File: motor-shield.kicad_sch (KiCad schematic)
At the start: 73 parts, among them J101 MC 1,5/ 2-G-3,5, J102 -, J103 MC 1,5/ 2-G-3,5, J104 -, J105 STEMMA QT, J106 Conn_02x04_smd, J107 Conn_01x04_f, Q101 AO3400A, Q102 AO3400A, SW101 Switch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

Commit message: Update to RevA1
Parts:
- removed FID101, FID102, FID103: Toolinghole_jlc, _my:toolinghole_jlc, symbol _my:Toolinghole_jlc
- removed FID104, FID105, FID106: Fiducial, Fiducial:Fiducial_1mm_Mask2mm, symbol Mechanical:Fiducial
- A101: footprint Module:Arduino_UNO_R3 -> _my:Arduino_UNO_R3_edit
- J107: footprint Connector_PinSocket_2.54mm:PinSocket_1x04_P2.54mm_Vertical -> _my:PinHeader_1x04_P2.54mm_Vertical_solderpad
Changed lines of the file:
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@@
     )
   )
-  (symbol (lib_id "_my:Toolinghole_jlc") (at 274.32 248.92 0) (unit 1)
-    (in_bom yes) (on_board yes) (dnp no) (fields_autoplaced)
-    (property "Reference" "FID101" (at 276.86 247.6499 0)
-      (effects (font (size 1.27 1.27)) (justify left))
-    )
-    (property "Value" "Toolinghole_jlc" (at 276.86 250.1899 0)
-      (effects (font (size 1.27 1.27)) (justify left))
-    )
-    (property "Footprint" "_my:toolinghole_jlc" (at 274.32 248.92 0)
-      (effects (font (size 1.27 1.27)) hide)
-    )
-    (property "Datasheet" "~" (at 274.32 248.92 0)
-      (effects (font (size 1.27 1.27)) hide)
-    )
-    (property "rohs_cert_or_in_datasheet" "" (at 274.32 248.92 0)
-      (effects (font (size 1.27 1.27)) hide)
-    )
-    (instances
-      (project "motor-shield"
-        (path "/0cbffc97-6856-4b34-94fa-39a0ff6f1c2b"
-          (reference "FID101") (unit 1)
-        )
-      )
-    )
-  )
   (symbol (lib_id "_my:IOREF") (at 137.16 227.33 0) (unit 1)
     (in_bom no) (on_board no) (dnp no)
@@
     )
   )
-  (symbol (lib_id "Mechanical:Fiducial") (at 274.32 266.7 0) (unit 1)
-    (in_bom yes) (on_board yes) (dnp no) (fields_autoplaced)
-    (property "Reference" "FID104" (at 276.86 265.4299 0)
-      (effects (font (size 1.27 1.27)) (justify left))
-    )
-    (property "Value" "Fiducial" (at 276.86 267.9699 0)
-      (effects (font (size 1.27 1.27)) (justify left))
-    )
-    (property "Footprint" "Fiducial:Fiducial_1mm_Mask2mm" (at 274.32 266.7 0)
-      (effects (font (size 1.27 1.27)) hide)
-    )
-    (property "Datasheet" "~" (at 274.32 266.7 0)
-      (effects (font (size 1.27 1.27)) hide)
-    )
-    (property "rohs_cert_or_in_datasheet" "" (at 274.32 266.7 0)
-      (effects (font (size 1.27 1.27)) hide)
-    )
-    (instances
-      (project "motor-shield"
-        (path "/0cbffc97-6856-4b34-94fa-39a0ff6f1c2b"
-          (reference "FID104") (unit 1)
-        )
-      )
-    )
-  )
   (symbol (lib_id "Connector_Generic:Conn_01x04") (at 370.84 203.2 0) (unit 1)
     (in_bom yes) (on_board yes) (dnp no) (fields_autoplaced)
@@
       (effects (font (size 1.27 1.27)) (justify left))
     )
-    (property "Footprint" "Connector_PinSocket_2.54mm:PinSocket_1x04_P2.54mm_Vertical" (at 370.84 203.2 0)
+    (property "Footprint" "_my:PinHeader_1x04_P2.54mm_Vertical_solderpad" (at 370.84 203.2 0)
       (effects (font (size 1.27 1.27)) hide)
     )
@@
       (effects (font (size 1.27 1.27)) (justify left))
     )
-    (property "Footprint" "Module:Arduino_UNO_R3" (at 57.15 69.85 0)
+    (property "Footprint" "_my:Arduino_UNO_R3_edit" (at 57.15 69.85 0)
       (effects (font (size 1.27 1.27) italic) hide)
     )
@@
     )
   )
-  (symbol (lib_id "Mechanical:Fiducial") (at 274.32 271.78 0) (unit 1)
-    (in_bom yes) (on_board yes) (dnp no) (fields_autoplaced)
-    (property "Reference" "FID105" (at 276.86 270.5099 0)
-      (effects (font (size 1.27 1.27)) (justify left))
-    )
-    (property "Value" "Fiducial" (at 276.86 273.0499 0)
-      (effects (font (size 1.27 1.27)) (justify left))
-    )
-    (property "Footprint" "Fiducial:Fiducial_1mm_Mask2mm" (at 274.32 271.78 0)
-      (effects (font (size 1.27 1.27)) hide)
-    )
-    (property "Datasheet" "~" (at 274.32 271.78 0)
-      (effects (font (size 1.27 1.27)) hide)
-    )
-    (property "rohs_cert_or_in_datasheet" "" (at 274.32 271.78 0)
-      (effects (font (size 1.27 1.27)) hide)
-    )
-    (instances
-      (project "motor-shield"
-        (path "/0cbffc97-6856-4b34-94fa-39a0ff6f1c2b"
-          (reference "FID105") (unit 1)
-        )
-      )
-    )
-  )
   (symbol (lib_id "Device:R_Small") (at 33.02 250.19 0) (unit 1)
     (in_bom yes) (on_board yes) (dnp no) (fields_autoplaced)
@@
     )
   )
-  (symbol (lib_id "_my:Toolinghole_jlc") (at 274.32 254 0) (unit 1)
-    (in_bom yes) (on_board yes) (dnp no) (fields_autoplaced)
-    (property "Reference" "FID102" (at 276.86 252.7299 0)
-      (effects (font (size 1.27 1.27)) (justify left))
-    )
-    (property "Value" "Toolinghole_jlc" (at 276.86 255.2699 0)
-      (effects (font (size 1.27 1.27)) (justify left))
-    )
-    (property "Footprint" "_my:toolinghole_jlc" (at 274.32 254 0)
-      (effects (font (size 1.27 1.27)) hide)
-    )
-    (property "Datasheet" "~" (at 274.32 254 0)
-      (effects (font (size 1.27 1.27)) hide)
-    )
-    (property "rohs_cert_or_in_datasheet" "" (at 274.32 254 0)
-      (effects (font (size 1.27 1.27)) hide)
-    )
-    (instances
-      (project "motor-shield"
-        (path "/0cbffc97-6856-4b34-94fa-39a0ff6f1c2b"
-          (reference "FID102") (unit 1)
-        )
-      )
-    )
-  )
   (symbol (lib_id "power:GND") (at 303.53 203.2 0) (unit 1)
     (in_bom yes) (on_board yes) (dnp no) (fields_autoplaced)
@@
     )
   )
-  (symbol (lib_id "_my:Toolinghole_jlc") (at 274.32 259.08 0) (unit 1)
-    (in_bom yes) (on_board yes) (dnp no) (fields_autoplaced)
-    (property "Reference" "FID103" (at 276.86 257.8099 0)
-      (effects (font (size 1.27 1.27)) (justify left))
-    )
-    (property "Value" "Toolinghole_jlc" (at 276.86 260.3499 0)
-      (effects (font (size 1.27 1.27)) (justify left))
-    )
-    (property "Footprint" "_my:toolinghole_jlc" (at 274.32 259.08 0)
-      (effects (font (size 1.27 1.27)) hide)
-    )
-    (property "Datasheet" "~" (at 274.32 259.08 0)
-      (effects (font (size 1.27 1.27)) hide)
-    )
-    (property "rohs_cert_or_in_datasheet" "" (at 274.32 259.08 0)
-      (effects (font (size 1.27 1.27)) hide)
-    )
-    (instances
-      (project "motor-shield"
-        (path "/0cbffc97-6856-4b34-94fa-39a0ff6f1c2b"
-          (reference "FID103") (unit 1)
-        )
-      )
-    )
-  )
   (symbol (lib_id "Device:R_Small") (at 232.41 43.18 0) (unit 1)
     (in_bom yes) (on_board yes) (dnp no)
@@
         )
       )
-    )
-  )
-  (symbol (lib_id "Mechanical:Fiducial") (at 274.32 276.86 0) (unit 1)
-    (in_bom yes) (on_board yes) (dnp no) (fields_autoplaced)
-    (property "Reference" "FID106" (at 276.86 275.5899 0)
-      (effects (font (size 1.27 1.27)) (justify left))
-    )
-    (property "Value" "Fiducial" (at 276.86 278.1299 0)
-      (effects (font (size 1.27 1.27)) (justify left))
-    )
-    (property "Footprint" "Fiducial:Fiducial_1mm_Mask2mm" (at 274.32 276.86 0)
-      (effects (font (size 1.27 1.27)) hide)
-    )
-    (property "Datasheet" "~" (at 274.32 276.86 0)
-      (effects (font (size 1.27 1.27)) hide)
-    )
-    (property "rohs_cert_or_in_datasheet" "" (at 274.32 276.86 0)
-      (effects (font (size 1.27 1.27)) hide)
-    )
-    (instances
-      (project "motor-shield"
-        (path "/0cbffc97-6856-4b34-94fa-39a0ff6f1c2b"
-          (reference "FID106") (unit 1)
-        )
-      )

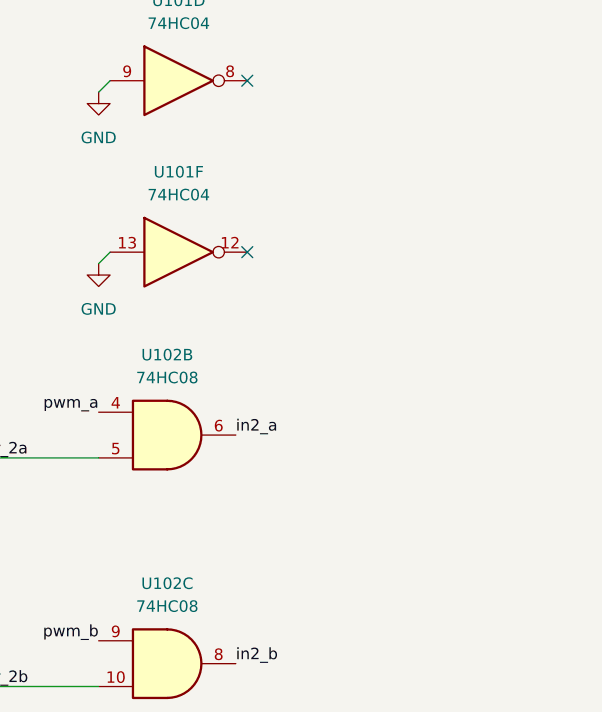
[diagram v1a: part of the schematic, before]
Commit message: Add pulldowns and make all pulldowns larger
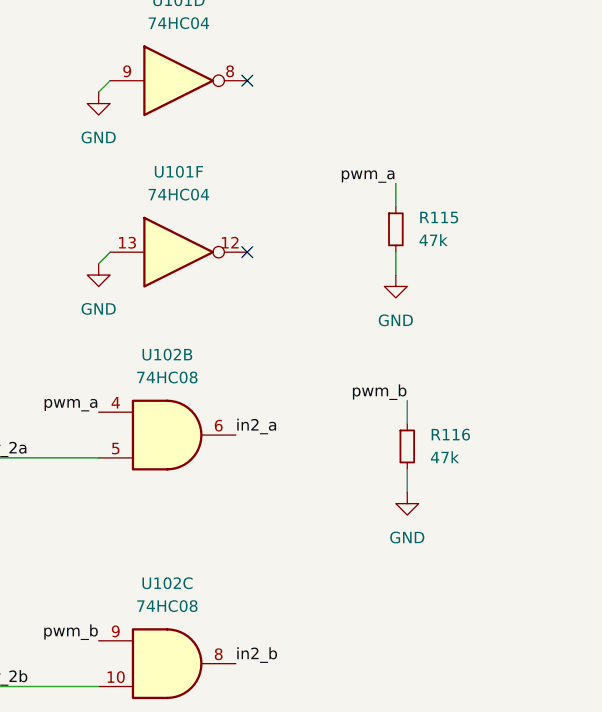
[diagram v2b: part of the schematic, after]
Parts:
- added R115, R116: 47k, Resistor_SMD:R_0603_1608Metric, symbol Device:R_Small
- R101, R102: footprint _my:R_1005_(0402) -> Resistor_SMD:R_0603_1608Metric
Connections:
- net GND: now also R115.2, R116.2
- net pwm_a: now also R115.1
- net pwm_b: now also R116.1
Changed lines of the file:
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@@
     (stroke (width 0) (type default))
   )
+  (wire (pts (xy 392.43 69.85) (xy 392.43 72.39))
+    (stroke (width 0) (type default))
+  )
   (wire (pts (xy 344.17 140.97) (xy 344.17 142.24))
     (stroke (width 0) (type default))
@@
     (stroke (width 0) (type default))
   )
+  (wire (pts (xy 391.16 40.64) (xy 391.16 38.1))
+    (stroke (width 0) (type default))
+  )
   (wire (pts (xy 382.27 180.34) (xy 382.27 179.07))
     (stroke (width 0) (type default))
@@
     (stroke (width 0) (type default))
   )
+  (wire (pts (xy 391.16 45.72) (xy 391.16 48.26))
+    (stroke (width 0) (type default))
+  )
+  (wire (pts (xy 392.43 64.77) (xy 392.43 62.23))
+    (stroke (width 0) (type default))
+  )
   (wire (pts (xy 54.61 99.06) (xy 57.15 99.06))
     (stroke (width 0) (type default))
@@
     (effects (font (size 1.27 1.27)) (justify right bottom))
   )
+  (label "pwm_b" (at 392.43 62.23 180) (fields_autoplaced)
+    (effects (font (size 1.27 1.27)) (justify right bottom))
+  )
   (label "brake_b_n" (at 143.51 165.1 0) (fields_autoplaced)
     (effects (font (size 1.27 1.27)) (justify left bottom))
@@
     (effects (font (size 1.27 1.27)) (justify left bottom))
   )
+  (label "pwm_a" (at 391.16 38.1 180) (fields_autoplaced)
+    (effects (font (size 1.27 1.27)) (justify right bottom))
+  )
   (label "fault_n_b" (at 82.55 163.83 0) (fields_autoplaced)
     (effects (font (size 1.27 1.27)) (justify left bottom))
@@
       (effects (font (size 1.27 1.27)) (justify left))
     )
-    (property "Footprint" "_my:R_1005_(0402)" (at 233.68 67.31 0)
+    (property "Footprint" "Resistor_SMD:R_0603_1608Metric" (at 233.68 67.31 0)
       (effects (font (size 1.27 1.27)) hide)
     )
@@
     )
   )
+  (symbol (lib_id "Device:R_Small") (at 392.43 67.31 0) (unit 1)
+    (in_bom yes) (on_board yes) (dnp no)
+    (property "Reference" "R116" (at 394.97 66.0399 0)
+      (effects (font (size 1.27 1.27)) (justify left))
+    )
+    (property "Value" "47k" (at 394.97 68.5799 0)
+      (effects (font (size 1.27 1.27)) (justify left))
+    )
+    (property "Footprint" "Resistor_SMD:R_0603_1608Metric" (at 392.43 67.31 0)
+      (effects (font (size 1.27 1.27)) hide)
+    )
+    (property "Datasheet" "~" (at 392.43 67.31 0)
+      (effects (font (size 1.27 1.27)) hide)
+    )
+    (property "LCSC Part #" "C163440" (at 392.43 67.31 0)
+      (effects (font (size 1.27 1.27)) hide)
+    )
+    (property "rohs_cert_or_in_datasheet" "y" (at 392.43 67.31 0)
+      (effects (font (size 1.27 1.27)) hide)
+    )
+    (pin "1")
+    (pin "2")
+    (instances
+      (project "motor-shield"
+        (path "/0cbffc97-6856-4b34-94fa-39a0ff6f1c2b"
+          (reference "R116") (unit 1)
+        )
+      )
+    )
+  )
   (symbol (lib_id "power:GND") (at 229.87 203.2 0) (unit 1)
     (in_bom yes) (on_board yes) (dnp no) (fields_autoplaced)
@@
     )
   )
+  (symbol (lib_id "power:GND") (at 391.16 48.26 0) (unit 1)
+    (in_bom yes) (on_board yes) (dnp no) (fields_autoplaced)
+    (property "Reference" "#PWR01" (at 391.16 54.61 0)
+      (effects (font (size 1.27 1.27)) hide)
+    )
+    (property "Value" "GND" (at 391.16 53.34 0)
+      (effects (font (size 1.27 1.27)))
+    )
+    (property "Footprint" "" (at 391.16 48.26 0)
+      (effects (font (size 1.27 1.27)) hide)
+    )
+    (property "Datasheet" "" (at 391.16 48.26 0)
+      (effects (font (size 1.27 1.27)) hide)
+    )
+    (pin "1")
+    (instances
+      (project "motor-shield"
+        (path "/0cbffc97-6856-4b34-94fa-39a0ff6f1c2b"
+          (reference "#PWR01") (unit 1)
+        )
+      )
+    )
+  )
   (symbol (lib_id "power:+5V") (at 25.4 242.57 0) (unit 1)
     (in_bom yes) (on_board yes) (dnp no) (fields_autoplaced)
@@
       (effects (font (size 1.27 1.27)) (justify left))
     )
-    (property "Footprint" "_my:R_1005_(0402)" (at 232.41 43.18 0)
+    (property "Footprint" "Resistor_SMD:R_0603_1608Metric" (at 232.41 43.18 0)
       (effects (font (size 1.27 1.27)) hide)
     )
@@
     )
   )
+  (symbol (lib_id "Device:R_Small") (at 391.16 43.18 0) (unit 1)
+    (in_bom yes) (on_board yes) (dnp no)
+    (property "Reference" "R115" (at 393.7 41.9099 0)
+      (effects (font (size 1.27 1.27)) (justify left))
+    )
+    (property "Value" "47k" (at 393.7 44.4499 0)
+      (effects (font (size 1.27 1.27)) (justify left))
+    )
+    (property "Footprint" "Resistor_SMD:R_0603_1608Metric" (at 391.16 43.18 0)
+      (effects (font (size 1.27 1.27)) hide)
+    )
+    (property "Datasheet" "~" (at 391.16 43.18 0)
+      (effects (font (size 1.27 1.27)) hide)
+    )
+    (property "LCSC Part #" "C163440" (at 391.16 43.18 0)
+      (effects (font (size 1.27 1.27)) hide)
+    )
+    (property "rohs_cert_or_in_datasheet" "y" (at 391.16 43.18 0)
+      (effects (font (size 1.27 1.27)) hide)
+    )
+    (pin "1")
+    (pin "2")
+    (instances
+      (project "motor-shield"
+        (path "/0cbffc97-6856-4b34-94fa-39a0ff6f1c2b"
+          (reference "R115") (unit 1)
+        )
+      )
+    )
+  )
   (symbol (lib_id "74xx:74HC04") (at 265.43 45.72 0) (unit 5)
     (in_bom yes) (on_board yes) (dnp no) (fields_autoplaced)
@@
         )
       )
+    )
+  )
+  (symbol (lib_id "power:GND") (at 392.43 72.39 0) (unit 1)
+    (in_bom yes) (on_board yes) (dnp no) (fields_autoplaced)
+    (property "Reference" "#PWR02" (at 392.43 78.74 0)
+      (effects (font (size 1.27 1.27)) hide)
+    )
+    (property "Value" "GND" (at 392.43 77.47 0)
+      (effects (font (size 1.27 1.27)))
+    )
+    (property "Footprint" "" (at 392.43 72.39 0)
+      (effects (font (size 1.27 1.27)) hide)
+    )
+    (property "Datasheet" "" (at 392.43 72.39 0)
+      (effects (font (size 1.27 1.27)) hide)
+    )
+    (pin "1")
+    (instances
+      (project "motor-shield"
+        (path "/0cbffc97-6856-4b34-94fa-39a0ff6f1c2b"
+          (reference "#PWR02") (unit 1)
+        )
+      )
